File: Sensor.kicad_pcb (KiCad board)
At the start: 2 copper layers, 49.5 x 49.5 mm, 48 parts, among them IC1 STM32L051K8T6, P1 CONN_02X04, P3 CONN_02X04, P4 CONN_01X04, P5 CONN_01X02, Q1 PMosfetGen, Q2 PMosfetGen, Q4 PMosfetGen, Q5 AO3401, SW1 SW_PUSH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

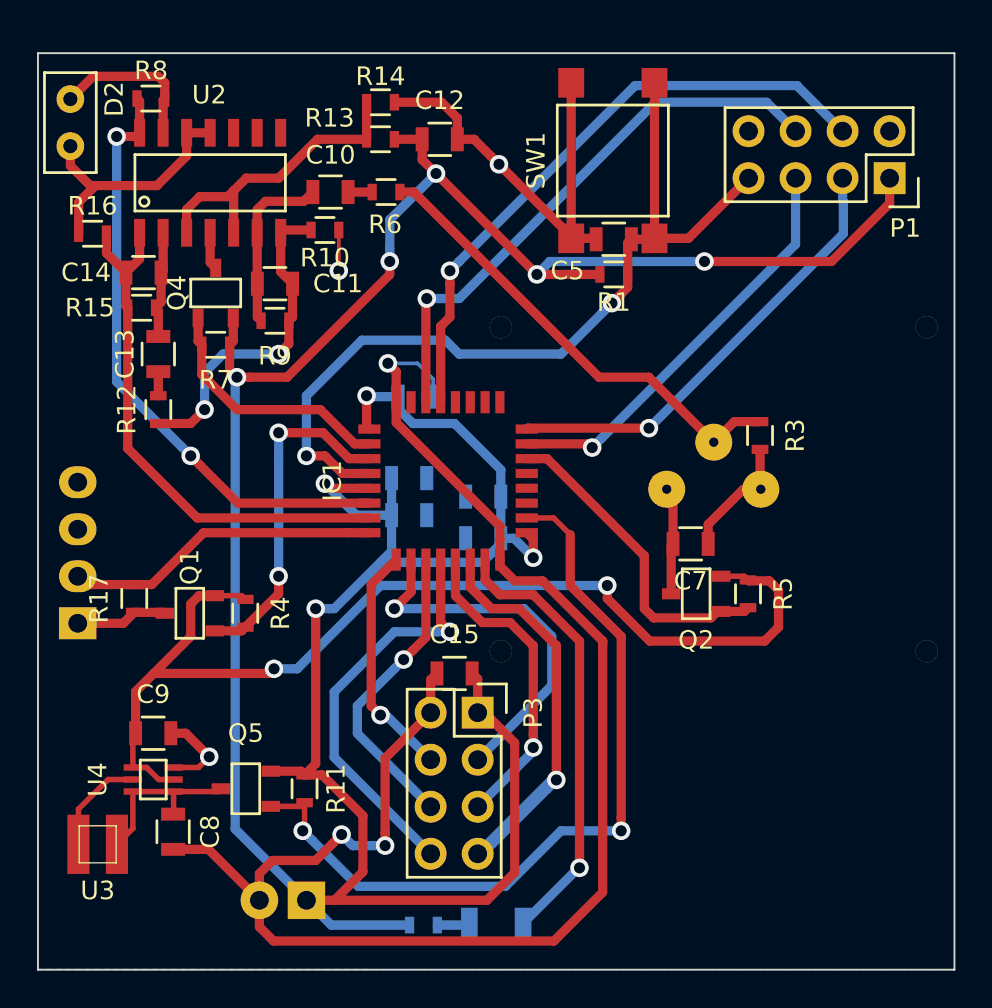
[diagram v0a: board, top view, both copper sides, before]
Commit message: Add M3 mounting holes
Signed-off-by: Philip Luyckx <philip.luyckx@gmail.com>
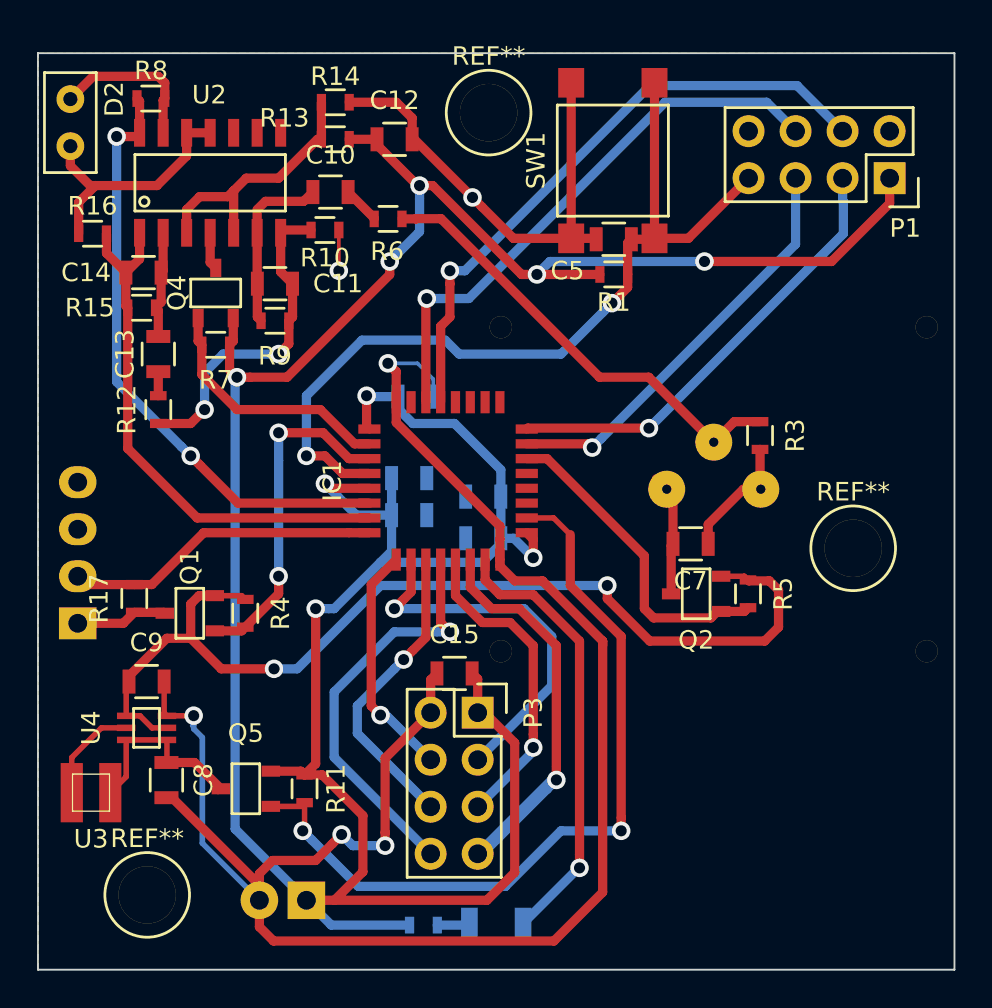
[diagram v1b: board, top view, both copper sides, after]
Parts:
- added REF**: 1pin, Connect:1pin, F.Cu at (142.8, 72.5)
- added REF**: 1pin, Connect:1pin, F.Cu at (124.4, 114.7)
- added REF**: 1pin, Connect:1pin, F.Cu at (162.5, 96.0)
- moved C8 2.81 mm to (125.4, 108.5)
- moved C9 2.81 mm to (124.4, 103.2)
- moved U3 2.81 mm to (121.4, 109.2)
- moved U4 2.81 mm to (124.4, 105.7)
- moved C12 2.44 mm to (137.8, 73.9)
- moved R13 2.44 mm to (134.6, 73.9)
- moved R14 2.44 mm to (134.6, 71.9)
- moved R6 1.45 mm to (137.4, 78.2)
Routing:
- net GND: track 136.4 -> 151.5 mm
- net +5V: track 58.9 -> 55.6 mm
- net Motion_Offset: track 16.8 -> 14.4 mm
- net Net-(C8-Pad1): track 9.25 -> 10.4 mm
- net +BATT: track 179.4 -> 180.3 mm
- net Net-(C10-Pad1): track 1.30 -> 2.03 mm
- net Motion_Out: track 25.5 -> 24.8 mm
